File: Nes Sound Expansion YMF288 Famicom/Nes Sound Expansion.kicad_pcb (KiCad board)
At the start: 2 copper layers, 67 x 99 mm, 29 parts, among them J1 OUT, J2 EXP 1-30, J3 EXP 1-30, J4 31-60, J8 EXP 25-48, J9 EXP 1-24, U1 74LS139, U10 74LS257, U2 74LS132, U6 74LS174, U7 74LS174, U8 74LS257, U9 74LS257, X1 CXO_DIP8

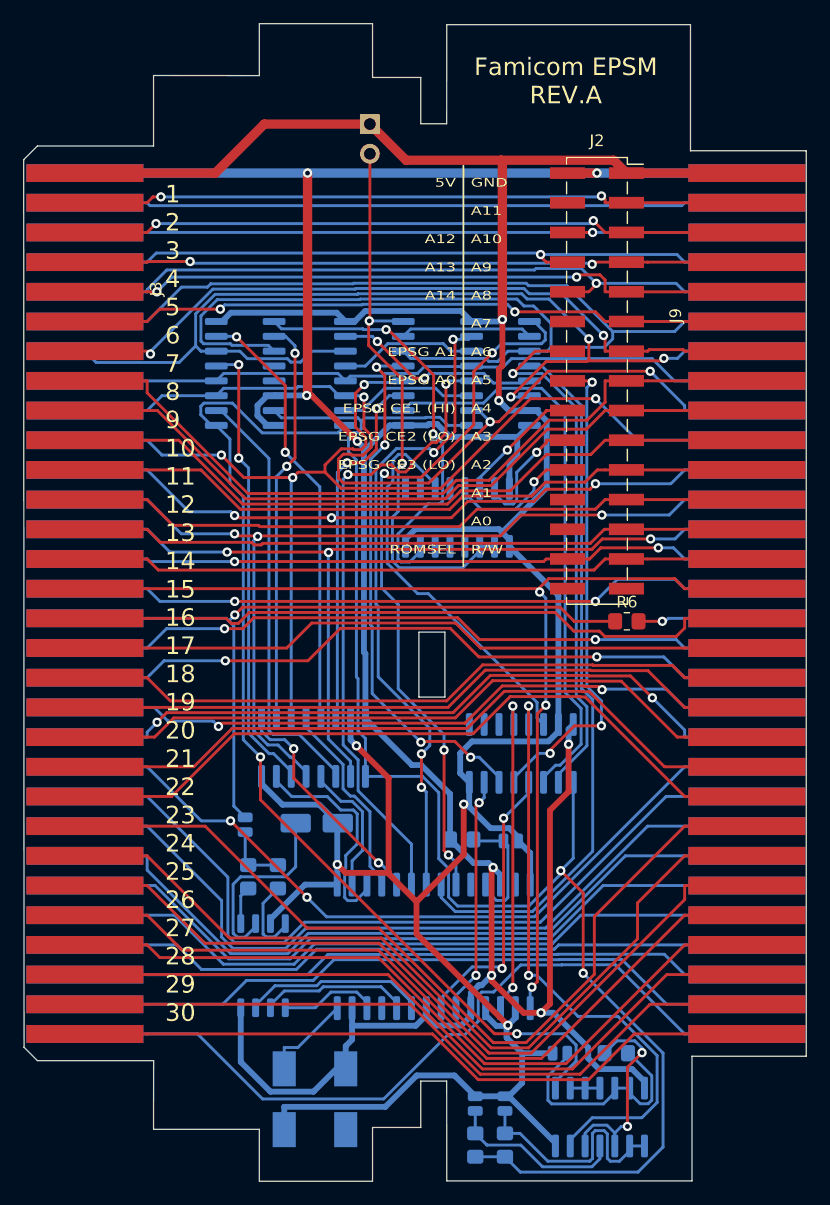
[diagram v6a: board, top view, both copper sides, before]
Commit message: Added amplification for both famicom and nes model
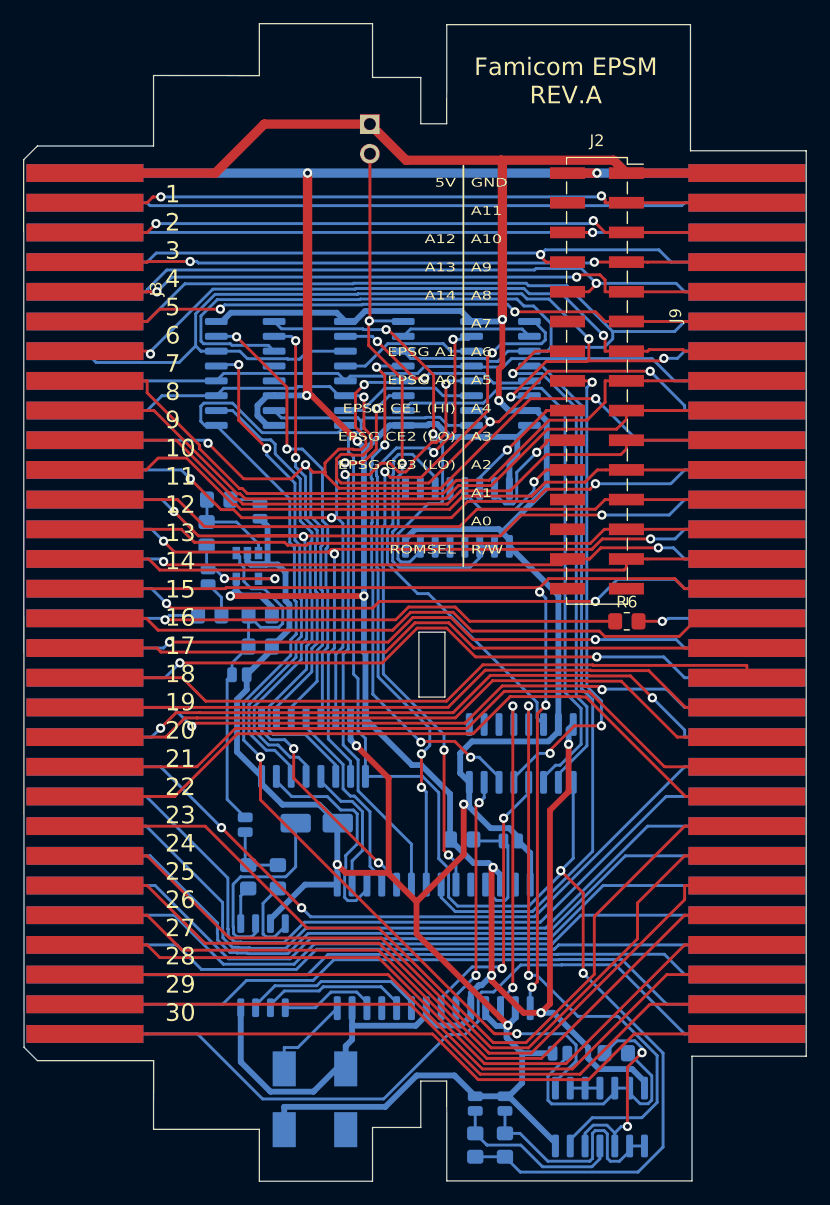
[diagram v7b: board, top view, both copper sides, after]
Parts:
- added C7: 68pF, Capacitor_SMD:C_0504_1310Metric_Pad0.83x1.28mm_HandSolder, B.Cu at (84.8, 88.6)
- added C8: 10uF, Capacitor_SMD:C_0504_1310Metric_Pad0.83x1.28mm_HandSolder, B.Cu at (86.6, 74.7)
- added C9: 10uF, Capacitor_SMD:C_0504_1310Metric_Pad0.83x1.28mm_HandSolder, B.Cu at (82.2, 80.3)
- added R1: 47k, Resistor_SMD:R_0805_2012Metric_Pad1.20x1.40mm_HandSolder, B.Cu at (86.6, 83.6)
- added R2: 47k, Resistor_SMD:R_0805_2012Metric_Pad1.20x1.40mm_HandSolder, B.Cu at (86.6, 86.2)
- added R3: 4.7k, Resistor_SMD:R_0805_2012Metric_Pad1.20x1.40mm_HandSolder, B.Cu at (83.1, 73.7)
- added R7: 47k, Resistor_SMD:R_0805_2012Metric_Pad1.20x1.40mm_HandSolder, B.Cu at (82.0, 76.6)
- added R9: 1k, Resistor_SMD:R_0805_2012Metric_Pad1.20x1.40mm_HandSolder, B.Cu at (82.3, 83.6)
- added U3: LM321, Package_TO_SOT_SMD:SOT-23-5, B.Cu at (85.5, 79.3)
- C6: value 1uF -> 10uF
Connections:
- C6 pad 2: AudIn -> Net-(C6-Pad2)
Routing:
- net Net-(C6-Pad2): track 0.00 -> 30.5 mm
- net GND: track 286.3 -> 316.5 mm
- net +5V: track 246.9 -> 264.4 mm, vias 8 -> 10
- net AudIn: track 63.8 -> 48.7 mm
- net Net-(C9-Pad2): track 0.00 -> 9.55 mm, vias 0 -> 2
- net Net-(R3-Pad1): track 0.00 -> 7.93 mm
- net D1: track 82.3 -> 88.4 mm
- net D0_buf: track 37.1 -> 41.6 mm
- net FF_Reset: track 90.0 -> 94.0 mm
- net D1_buf: track 39.3 -> 43.2 mm
- net D3: track 98.2 -> 101.9 mm
- net Net-(C9-Pad1): track 0.00 -> 3.15 mm
- net Net-(C8-Pad1): track 0.00 -> 2.70 mm
- net D3_buf: track 34.7 -> 36.7 mm
- net D2_buf: track 37.4 -> 38.8 mm
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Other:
- net class Power: trace_width 0.8 -> 0.5

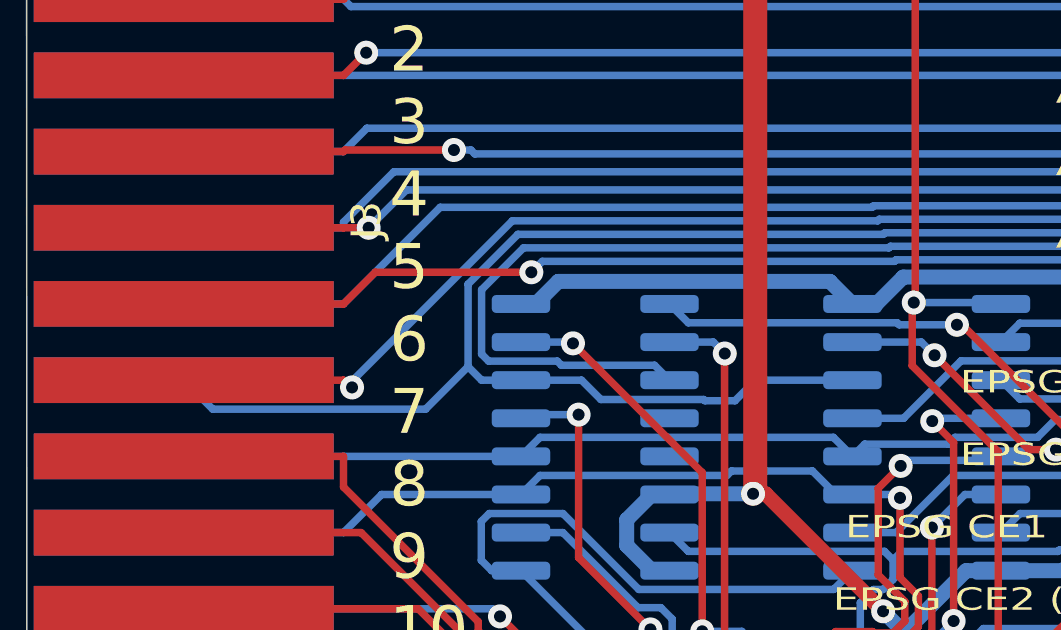
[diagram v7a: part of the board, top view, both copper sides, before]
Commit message: Updated 401C-F addressing circuit
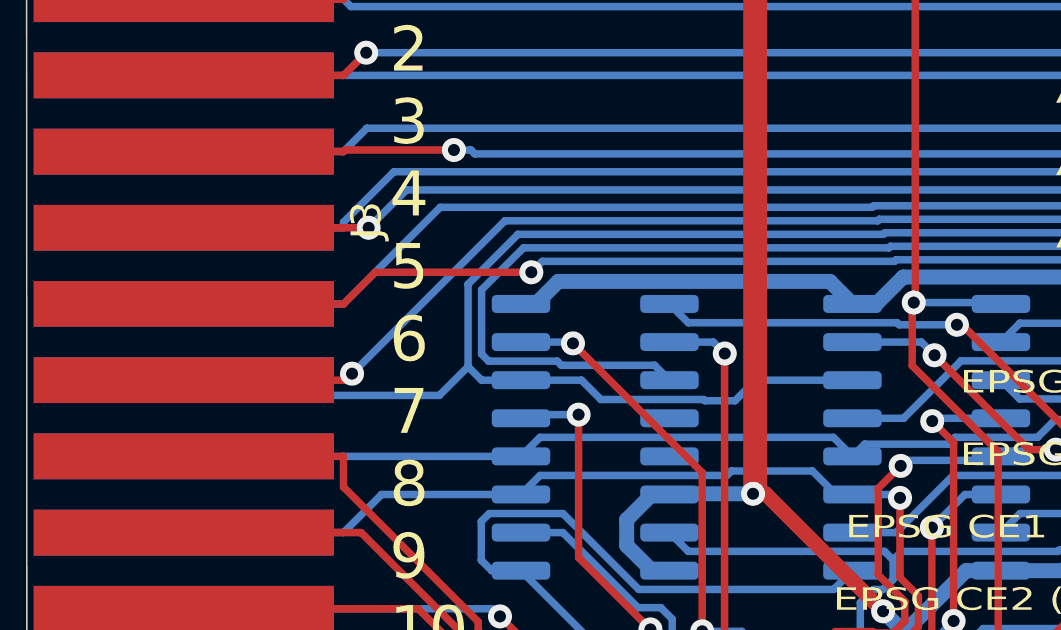
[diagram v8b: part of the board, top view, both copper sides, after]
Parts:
- added G***: LOGO, Nes Sound Expansion OPNA:EPSM Logo, B.Cu at (113.1, 38.1)
